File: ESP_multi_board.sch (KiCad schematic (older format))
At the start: 20 parts, among them P101 CONN_01X02, P102 CONN_01X06, P103 CONN_01X02, P104 CONN_01X06, P105 CONN_01X12, P106 CONN_01X03, P107 JUMPER1, P108 CONN_I2C_MPU6050, P109 CONN_01X03, P110 CONN_01X03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

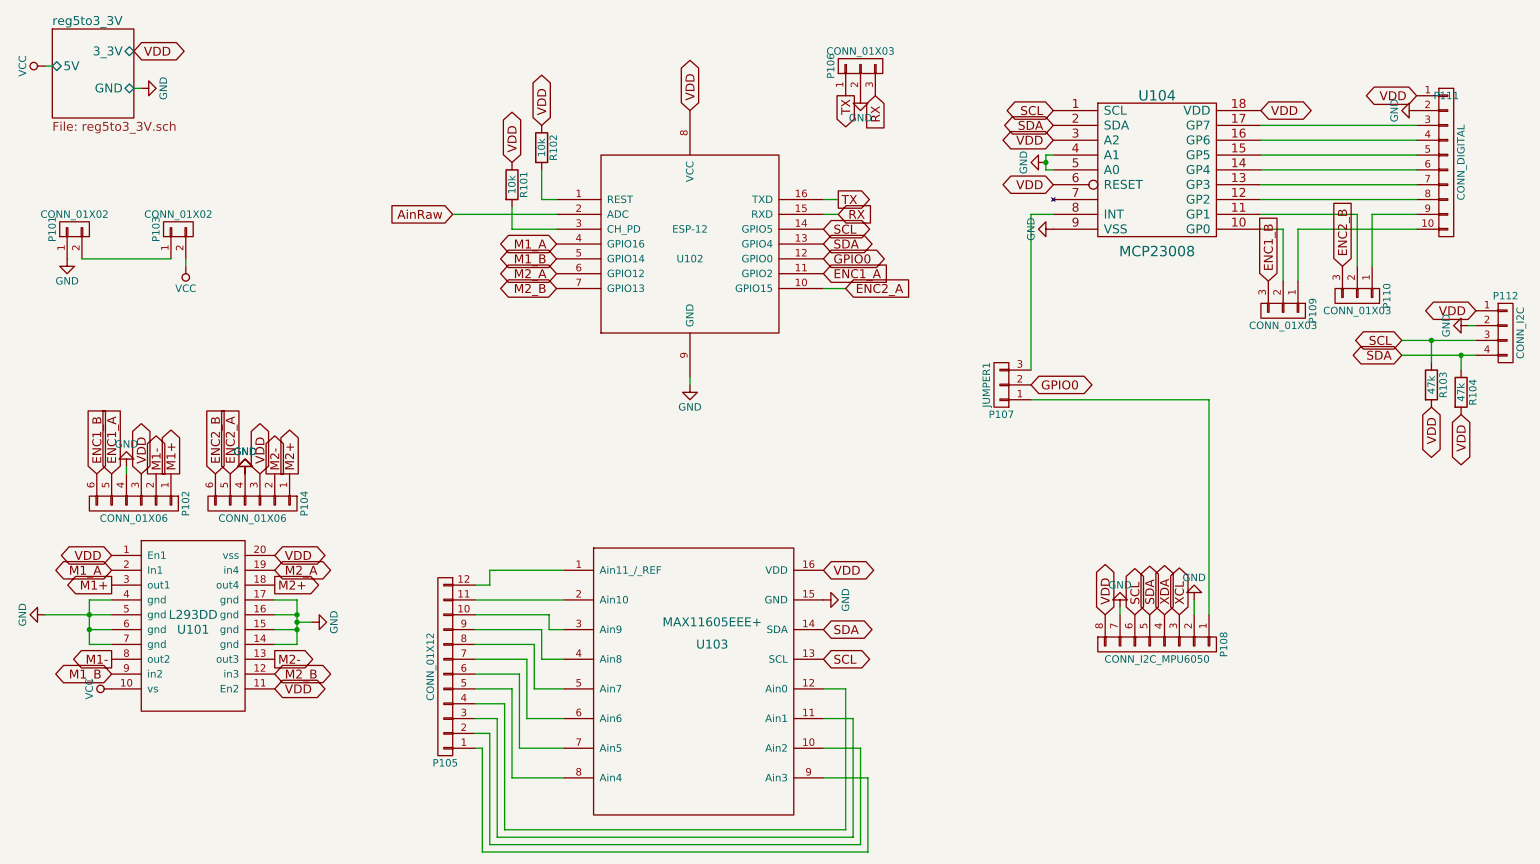
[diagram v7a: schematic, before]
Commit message: actualizaciones en CRM. TODO: cambiar L293DD por L298smd, cambiar para controlar ENs con pwm, y pines de direccion de motores desde el extensor de pines, eliminar jumpers, ajustar tamaño de las resistencias
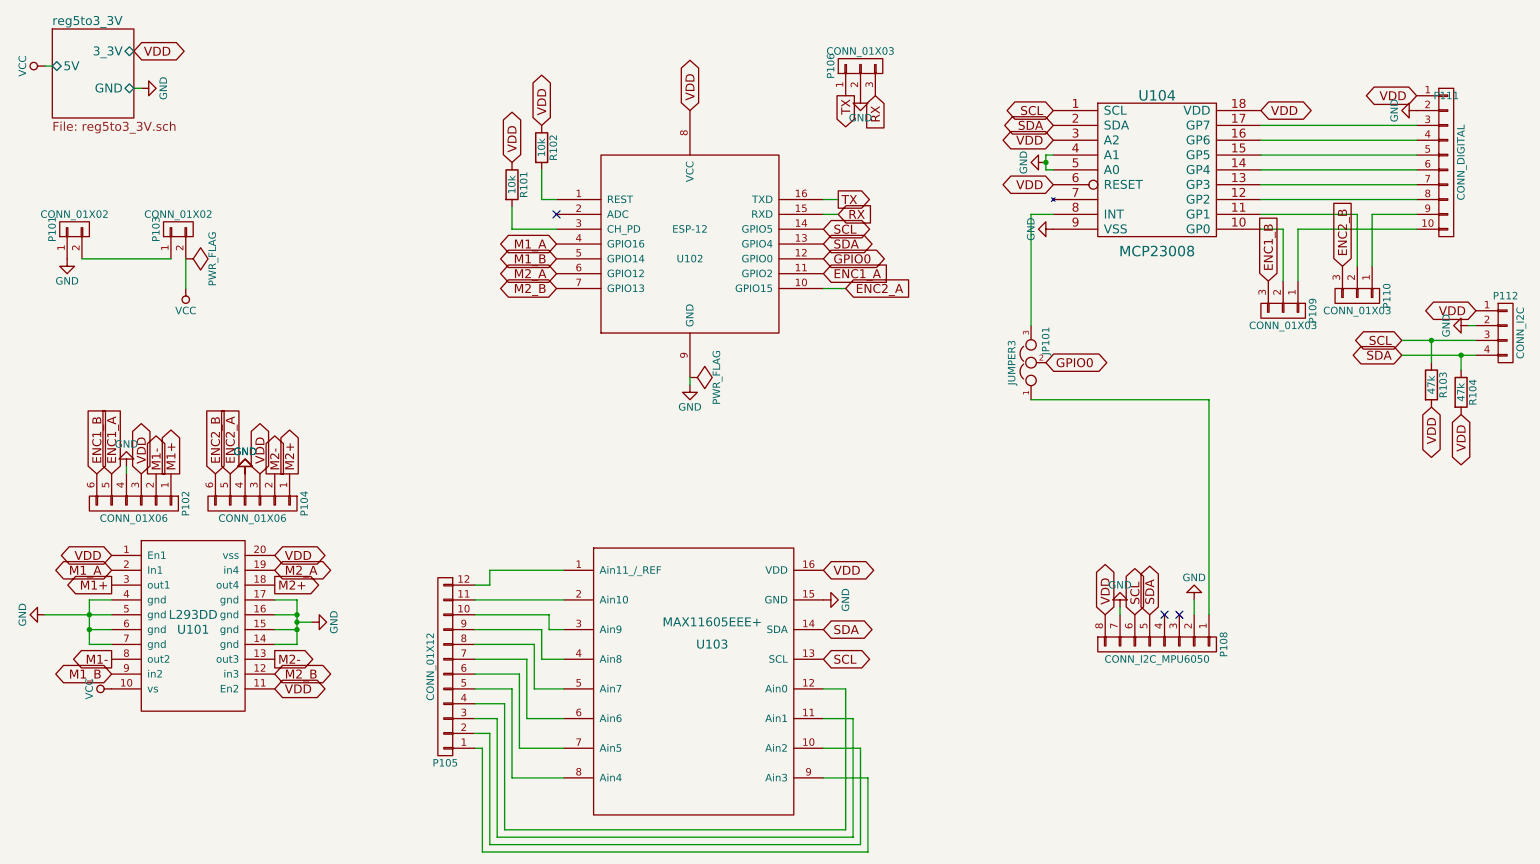
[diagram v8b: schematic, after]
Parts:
- removed P107: JUMPER1, Pin_Headers:Pin_Header_Straight_1x03, symbol CONN_01X03
- added JP101: JUMPER3, Oddities:NetTie-II_SMD, symbol JUMPER3
- R101, R102, R103, R104: footprint Resistors_SMD:R_0402 -> Resistors_SMD:R_1812_HandSoldering
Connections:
- net GPIO0: now also JP101.2
- net at U104.8 (INT): now also JP101.3
- net at P108.1 (P1): now also JP101.1
- net AinRaw: no longer names the net of U102.2 (ADC)
- net XCL: no longer names the net of P108.3 (P3)
- net XDA: no longer names the net of P108.4 (P4)
- no-connect marks 0 -> 3
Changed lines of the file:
@@
 $EndComp
 $Comp
-L VCC #PWR09
-U 1 1 57125BED
-P 1900 2400
-F 0 "#PWR09" H 1900 2250 50  0001 C CNN
-F 1 "VCC" H 1900 2550 50  0000 C CNN
-F 2 "" H 1900 2400 50  0000 C CNN
-F 3 "" H 1900 2400 50  0000 C CNN
-	1    1900 2400
-	-1   0    0    1
-$EndComp
-$Comp
-L GND #PWR010
+L GND #PWR09
 U 1 1 57125BEE
 P 1100 2350
-F 0 "#PWR010" H 1100 2100 50  0001 C CNN
+F 0 "#PWR09" H 1100 2100 50  0001 C CNN
 F 1 "GND" H 1100 2200 50  0000 C CNN
 F 2 "" H 1100 2350 50  0000 C CNN
@@
 F 0 "R102" V 4380 1600 50  0000 C CNN
 F 1 "10k" V 4300 1600 50  0000 C CNN
-F 2 "Resistors_SMD:R_0402" V 4230 1600 50  0001 C CNN
+F 2 "Resistors_SMD:R_1812_HandSoldering" V 4230 1600 50  0001 C CNN
 F 3 "" H 4300 1600 50  0000 C CNN
 	1    4300 1600
@@
 F 0 "R101" V 4180 1850 50  0000 C CNN
 F 1 "10k" V 4100 1850 50  0000 C CNN
-F 2 "Resistors_SMD:R_0402" V 4030 1850 50  0001 C CNN
+F 2 "Resistors_SMD:R_1812_HandSoldering" V 4030 1850 50  0001 C CNN
 F 3 "" H 4100 1850 50  0000 C CNN
 	1    4100 1850
@@
 Text GLabel 6300 1950 2    60   Output ~ 0
 TX
-Text GLabel 3700 2050 0    60   Input ~ 0
-AinRaw
 $Comp
 L CONN_01X04 P112
@@
 F 0 "R104" V 10580 3250 50  0000 C CNN
 F 1 "47k" V 10500 3250 50  0000 C CNN
-F 2 "Resistors_SMD:R_0402" V 10430 3250 50  0001 C CNN
+F 2 "Resistors_SMD:R_1812_HandSoldering" V 10430 3250 50  0001 C CNN
 F 3 "" H 10500 3250 50  0000 C CNN
 	1    10500 3250
@@
 F 0 "R103" V 10380 3200 50  0000 C CNN
 F 1 "47k" V 10300 3200 50  0000 C CNN
-F 2 "Resistors_SMD:R_0402" V 10230 3200 50  0001 C CNN
+F 2 "Resistors_SMD:R_1812_HandSoldering" V 10230 3200 50  0001 C CNN
 F 3 "" H 10300 3200 50  0000 C CNN
 	1    10300 3200
@@
 Text GLabel 8400 4750 1    60   BiDi ~ 0
 SDA
-Text GLabel 8500 4750 1    60   BiDi ~ 0
-XDA
-Text GLabel 8600 4750 1    60   BiDi ~ 0
-XCL
-$Comp
-L CONN_01X03 P107
-U 1 1 5713DB4D
-P 7400 3200
-F 0 "P107" H 7400 3400 50  0000 C CNN
-F 1 "JUMPER1" V 7500 3200 50  0000 C CNN
-F 2 "Pin_Headers:Pin_Header_Straight_1x03" H 7400 3200 50  0001 C CNN
-F 3 "" H 7400 3200 50  0000 C CNN
-	1    7400 3200
-	-1   0    0    1
-$EndComp
-Text GLabel 7600 3200 2    60   BiDi ~ 0
+Text GLabel 7700 3050 2    60   BiDi ~ 0
 GPIO0
 Text GLabel 7750 1850 0    60   BiDi ~ 0
@@
 M1+
 $Comp
-L GND #PWR011
+L GND #PWR010
 U 1 1 57143D77
 P 10200 1350
-F 0 "#PWR011" H 10200 1100 50  0001 C CNN
+F 0 "#PWR010" H 10200 1100 50  0001 C CNN
 F 1 "GND" H 10200 1200 50  0000 C CNN
 F 2 "" H 10200 1350 50  0000 C CNN
@@
 $EndComp
 $Comp
-L GND #PWR012
+L GND #PWR011
 U 1 1 57144505
 P 8700 4650
-F 0 "#PWR012" H 8700 4400 50  0001 C CNN
+F 0 "#PWR011" H 8700 4400 50  0001 C CNN
 F 1 "GND" H 8700 4500 50  0000 C CNN
 F 2 "" H 8700 4650 50  0000 C CNN
@@
 $EndComp
 $Comp
-L GND #PWR013
+L GND #PWR012
 U 1 1 571445C1
 P 8200 4700
-F 0 "#PWR013" H 8200 4450 50  0001 C CNN
+F 0 "#PWR012" H 8200 4450 50  0001 C CNN
 F 1 "GND" H 8200 4550 50  0000 C CNN
 F 2 "" H 8200 4700 50  0000 C CNN
@@
 $EndComp
 $Comp
-L GND #PWR014
+L GND #PWR013
 U 1 1 5714467D
 P 10550 2800
-F 0 "#PWR014" H 10550 2550 50  0001 C CNN
+F 0 "#PWR013" H 10550 2550 50  0001 C CNN
 F 1 "GND" H 10550 2650 50  0000 C CNN
 F 2 "" H 10550 2800 50  0000 C CNN
@@
 $EndComp
 $Comp
-L GND #PWR015
+L GND #PWR014
 U 1 1 5714473B
 P 7750 2150
-F 0 "#PWR015" H 7750 1900 50  0001 C CNN
+F 0 "#PWR014" H 7750 1900 50  0001 C CNN
 F 1 "GND" H 7750 2000 50  0000 C CNN
 F 2 "" H 7750 2150 50  0000 C CNN
@@
 TX
 $Comp
-L GND #PWR016
+L GND #PWR015
 U 1 1 57146199
 P 6450 1250
-F 0 "#PWR016" H 6450 1000 50  0001 C CNN
+F 0 "#PWR015" H 6450 1000 50  0001 C CNN
 F 1 "GND" H 6450 1100 50  0000 C CNN
 F 2 "" H 6450 1250 50  0000 C CNN
@@
 M2_B
 $Comp
-L GND #PWR017
+L GND #PWR016
 U 1 1 5714055F
 P 2750 4800
-F 0 "#PWR017" H 2750 4550 50  0001 C CNN
+F 0 "#PWR016" H 2750 4550 50  0001 C CNN
 F 1 "GND" H 2750 4650 50  0000 C CNN
 F 2 "" H 2750 4800 50  0000 C CNN
@@
 	10200 1450 9150 1450
 Wire Wire Line
-	7600 2050 7600 3100
+	7600 2050 7600 2800
 Wire Wire Line
 	1200 2350 1800 2350
@@
 Wire Wire Line
 	4100 2150 4100 2000
-Wire Wire Line
-	4400 2050 3700 2050
 Wire Wire Line
 	10100 3000 10600 3000
@@
 	8200 4700 8200 4750
 Wire Wire Line
-	1900 2350 1900 2400
-Wire Wire Line
 	9150 2150 9300 2150
 Wire Wire Line
@@
 Connection ~ 2650 4800
 $Comp
-L GND #PWR018
+L GND #PWR017
 U 1 1 57140F36
 P 950 4750
-F 0 "#PWR018" H 950 4500 50  0001 C CNN
+F 0 "#PWR017" H 950 4500 50  0001 C CNN
 F 1 "GND" H 950 4600 50  0000 C CNN
 F 2 "" H 950 4750 50  0000 C CNN
@@
 M1+
 $Comp
-L VCC #PWR019
+L VCC #PWR018
 U 1 1 57140F40
 P 1400 5250
-F 0 "#PWR019" H 1400 5100 50  0001 C CNN
+F 0 "#PWR018" H 1400 5100 50  0001 C CNN
 F 1 "VCC" H 1400 5400 50  0000 C CNN
 F 2 "" H 1400 5250 50  0000 C CNN
@@
 Wire Wire Line
 	6500 5850 6200 5850
+$Comp
+L JUMPER3 JP101
+U 1 1 571538C5
+P 7600 3050
+F 0 "JP101" H 7650 2950 50  0000 L CNN
+F 1 "JUMPER3" H 7600 3150 50  0000 C BNN
+F 2 "Oddities:NetTie-II_SMD" H 7600 3050 50  0001 C CNN
+F 3 "" H 7600 3050 50  0000 C CNN
+	1    7600 3050
+	0    -1   -1   0
+$EndComp
+$Comp
+L PWR_FLAG #FLG019
+U 1 1 57154A7C
+P 1900 2350
+F 0 "#FLG019" H 1900 2445 50  0001 C CNN
+F 1 "PWR_FLAG" H 1900 2530 50  0000 C CNN
+F 2 "" H 1900 2350 50  0000 C CNN
+F 3 "" H 1900 2350 50  0000 C CNN
+	1    1900 2350
+	0    1    1    0
+$EndComp
+$Comp
+L VCC #PWR020
+U 1 1 57154E13
+P 1900 2550
+F 0 "#PWR020" H 1900 2400 50  0001 C CNN
+F 1 "VCC" H 1900 2700 50  0000 C CNN
+F 2 "" H 1900 2550 50  0000 C CNN
+F 3 "" H 1900 2550 50  0000 C CNN
+	1    1900 2550
+	-1   0    0    1
+$EndComp
+Wire Wire Line
+	1900 2350 1900 2550
+$Comp
+L PWR_FLAG #FLG021
+U 1 1 571554D1
+P 5300 3150
+F 0 "#FLG021" H 5300 3245 50  0001 C CNN
+F 1 "PWR_FLAG" H 5300 3330 50  0000 C CNN
+F 2 "" H 5300 3150 50  0000 C CNN
+F 3 "" H 5300 3150 50  0000 C CNN
+	1    5300 3150
+	0    1    1    0
+$EndComp
+NoConn ~ 4400 2050
+NoConn ~ 8500 4750
+NoConn ~ 8600 4750
 $EndSCHEMATC
